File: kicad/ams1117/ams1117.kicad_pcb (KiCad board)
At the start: 2 copper layers, 18.5 x 10.5 mm, 4 parts, among them J1 Conn_01x03

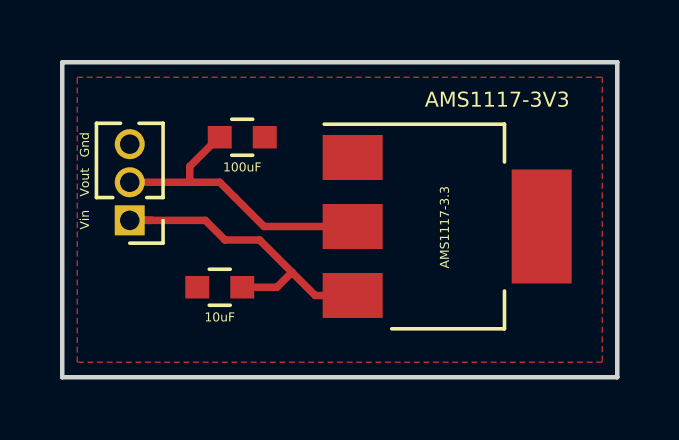
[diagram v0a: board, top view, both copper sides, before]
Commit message: AMS1117: Add way to thermal vias
This is based on https://www.youtube.com/watch?v=Hp5ngKtl7S4
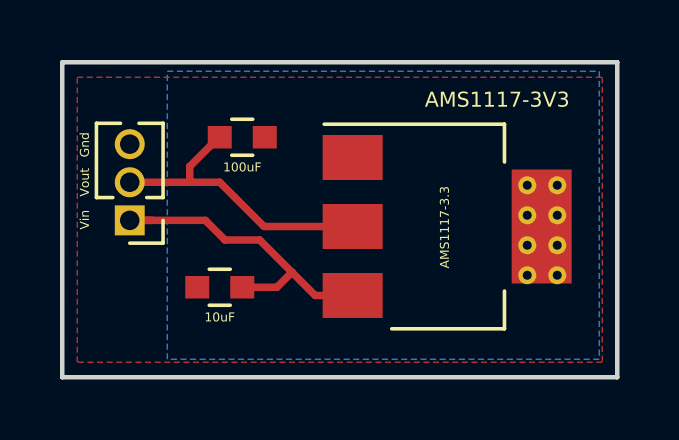
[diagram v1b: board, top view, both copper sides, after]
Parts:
- added REF**: VIA-0.6mm, via:VIA-0.6mm, F.Cu at (155.0, 107.6)
- added REF**: VIA-0.6mm, via:VIA-0.6mm, F.Cu at (155.0, 106.6)
- added REF**: VIA-0.6mm, via:VIA-0.6mm, F.Cu at (154.0, 106.6)
- added REF**: VIA-0.6mm, via:VIA-0.6mm, F.Cu at (155.0, 105.6)
- added REF**: VIA-0.6mm, via:VIA-0.6mm, F.Cu at (154.0, 105.6)
- added REF**: VIA-0.6mm, via:VIA-0.6mm, F.Cu at (155.0, 104.6)
- added REF**: VIA-0.6mm, via:VIA-0.6mm, F.Cu at (154.0, 107.6)
- added REF**: VIA-0.6mm, via:VIA-0.6mm, F.Cu at (154.0, 104.6)
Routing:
- added copper zone on B.Cu, net Net-(U1-Pad4)
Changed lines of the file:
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@@
-(kicad_pcb (version 4) (host pcbnew 4.0.7-e2-6376~58~ubuntu16.04.1)
+(kicad_pcb (version 4) (host pcbnew 4.0.7)
   (general
-    (links 7)
+    (links 8)
     (no_connects 0)
     (area 138.424999 100.424999 157.075001 111.075001)
@@
     (tracks 19)
     (zones 0)
-    (modules 4)
+    (modules 12)
     (nets 5)
   )
@@
     (mod_text_size 1 1)
     (mod_text_width 0.15)
-    (pad_size 1.524 1.524)
-    (pad_drill 0.762)
+    (pad_size 0.6 0.6)
+    (pad_drill 0.3)
     (pad_to_mask_clearance 0.2)
     (aux_axis_origin 0 0)
@@
     (add_net "Net-(U1-Pad4)")
   )
+  (module via:VIA-0.6mm (layer F.Cu)
+    (at 155 107.6)
+    (fp_text reference REF** (at 0 1.27) (layer F.SilkS) hide
+      (effects (font (size 1 1) (thickness 0.15)))
+    )
+    (fp_text value VIA-0.6mm (at 0 -1.27) (layer F.Fab) hide
+      (effects (font (size 1 1) (thickness 0.15)))
+    )
+    (pad 1 thru_hole circle (at 0 0) (size 0.6 0.6) (drill 0.3) (layers *.Cu)
+      (net 4 "Net-(U1-Pad4)") (zone_connect 2))
+  )
+  (module via:VIA-0.6mm (layer F.Cu)
+    (at 155 106.6)
+    (fp_text reference REF** (at 0 1.27) (layer F.SilkS) hide
+      (effects (font (size 1 1) (thickness 0.15)))
+    )
+    (fp_text value VIA-0.6mm (at 0 -1.27) (layer F.Fab) hide
+      (effects (font (size 1 1) (thickness 0.15)))
+    )
+    (pad 1 thru_hole circle (at 0 0) (size 0.6 0.6) (drill 0.3) (layers *.Cu)
+      (net 4 "Net-(U1-Pad4)") (zone_connect 2))
+  )
+  (module via:VIA-0.6mm (layer F.Cu)
+    (at 154 106.6)
+    (fp_text reference REF** (at 0 1.27) (layer F.SilkS) hide
+      (effects (font (size 1 1) (thickness 0.15)))
+    )
+    (fp_text value VIA-0.6mm (at 0 -1.27) (layer F.Fab) hide
+      (effects (font (size 1 1) (thickness 0.15)))
+    )
+    (pad 1 thru_hole circle (at 0 0) (size 0.6 0.6) (drill 0.3) (layers *.Cu)
+      (net 4 "Net-(U1-Pad4)") (zone_connect 2))
+  )
+  (module via:VIA-0.6mm (layer F.Cu)
+    (at 155 105.6)
+    (fp_text reference REF** (at 0 1.27) (layer F.SilkS) hide
+      (effects (font (size 1 1) (thickness 0.15)))
+    )
+    (fp_text value VIA-0.6mm (at 0 -1.27) (layer F.Fab) hide
+      (effects (font (size 1 1) (thickness 0.15)))
+    )
+    (pad 1 thru_hole circle (at 0 0) (size 0.6 0.6) (drill 0.3) (layers *.Cu)
+      (net 4 "Net-(U1-Pad4)") (zone_connect 2))
+  )
+  (module via:VIA-0.6mm (layer F.Cu)
+    (at 154 105.6)
+    (fp_text reference REF** (at 0 1.27) (layer F.SilkS) hide
+      (effects (font (size 1 1) (thickness 0.15)))
+    )
+    (fp_text value VIA-0.6mm (at 0 -1.27) (layer F.Fab) hide
+      (effects (font (size 1 1) (thickness 0.15)))
+    )
+    (pad 1 thru_hole circle (at 0 0) (size 0.6 0.6) (drill 0.3) (layers *.Cu)
+      (net 4 "Net-(U1-Pad4)") (zone_connect 2))
+  )
+  (module via:VIA-0.6mm (layer F.Cu)
+    (at 155 104.6)
+    (fp_text reference REF** (at 0 1.27) (layer F.SilkS) hide
+      (effects (font (size 1 1) (thickness 0.15)))
+    )
+    (fp_text value VIA-0.6mm (at 0 -1.27) (layer F.Fab) hide
+      (effects (font (size 1 1) (thickness 0.15)))
+    )
+    (pad 1 thru_hole circle (at 0 0) (size 0.6 0.6) (drill 0.3) (layers *.Cu)
+      (net 4 "Net-(U1-Pad4)") (zone_connect 2))
+  )
+  (module via:VIA-0.6mm (layer F.Cu)
+    (at 154 107.6)
+    (fp_text reference REF** (at 0 1.27) (layer F.SilkS) hide
+      (effects (font (size 1 1) (thickness 0.15)))
+    )
+    (fp_text value VIA-0.6mm (at 0 -1.27) (layer F.Fab) hide
+      (effects (font (size 1 1) (thickness 0.15)))
+    )
+    (pad 1 thru_hole circle (at 0 0) (size 0.6 0.6) (drill 0.3) (layers *.Cu)
+      (net 4 "Net-(U1-Pad4)") (zone_connect 2))
+  )
   (module Capacitors_SMD:C_0603 (layer F.Cu)
     (at 143.75 108 180)
@@
       (rotate (xyz 0 0 0))
     )
+  )
+  (module via:VIA-0.6mm (layer F.Cu)
+    (at 154 104.6)
+    (fp_text reference REF** (at 0 1.27) (layer F.SilkS) hide
+      (effects (font (size 1 1) (thickness 0.15)))
+    )
+    (fp_text value VIA-0.6mm (at 0 -1.27) (layer F.Fab) hide
+      (effects (font (size 1 1) (thickness 0.15)))
+    )
+    (pad 1 thru_hole circle (at 0 0) (size 0.6 0.6) (drill 0.3) (layers *.Cu)
+      (net 4 "Net-(U1-Pad4)") (zone_connect 2))
   )
   (gr_text Gnd (at 139.25 103.25 90) (layer F.SilkS)
@@
       )
     )
+  )
+  (zone (net 4) (net_name "Net-(U1-Pad4)") (layer B.Cu) (hatch edge 0.508)
+    (connect_pads (clearance 0.508))
+    (min_thickness 0.254)
+    (fill yes (arc_segments 16) (thermal_gap 0.508) (thermal_bridge_width 0.508))
+    (polygon
+      (pts
+        (xy 142 100.8) (xy 156.4 100.8) (xy 156.4 110.4) (xy 142 110.4)
+      )
+    )
